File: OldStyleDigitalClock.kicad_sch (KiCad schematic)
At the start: 81 parts, among them SW1 Set minutes, SW2 Set hours, U1 D168K, U10 D168K, U11 CD4026BE, U12 D168K, U13 CD4026BE, U2 CD4026BE, U3 CD4060BE, U4 D168K, U5 CD4026BE, U6 CD4017BE, U7 CD4017BE, U8 CD4017BE, U9 4073, Y1 HC49 XTAL (32768 Hz)

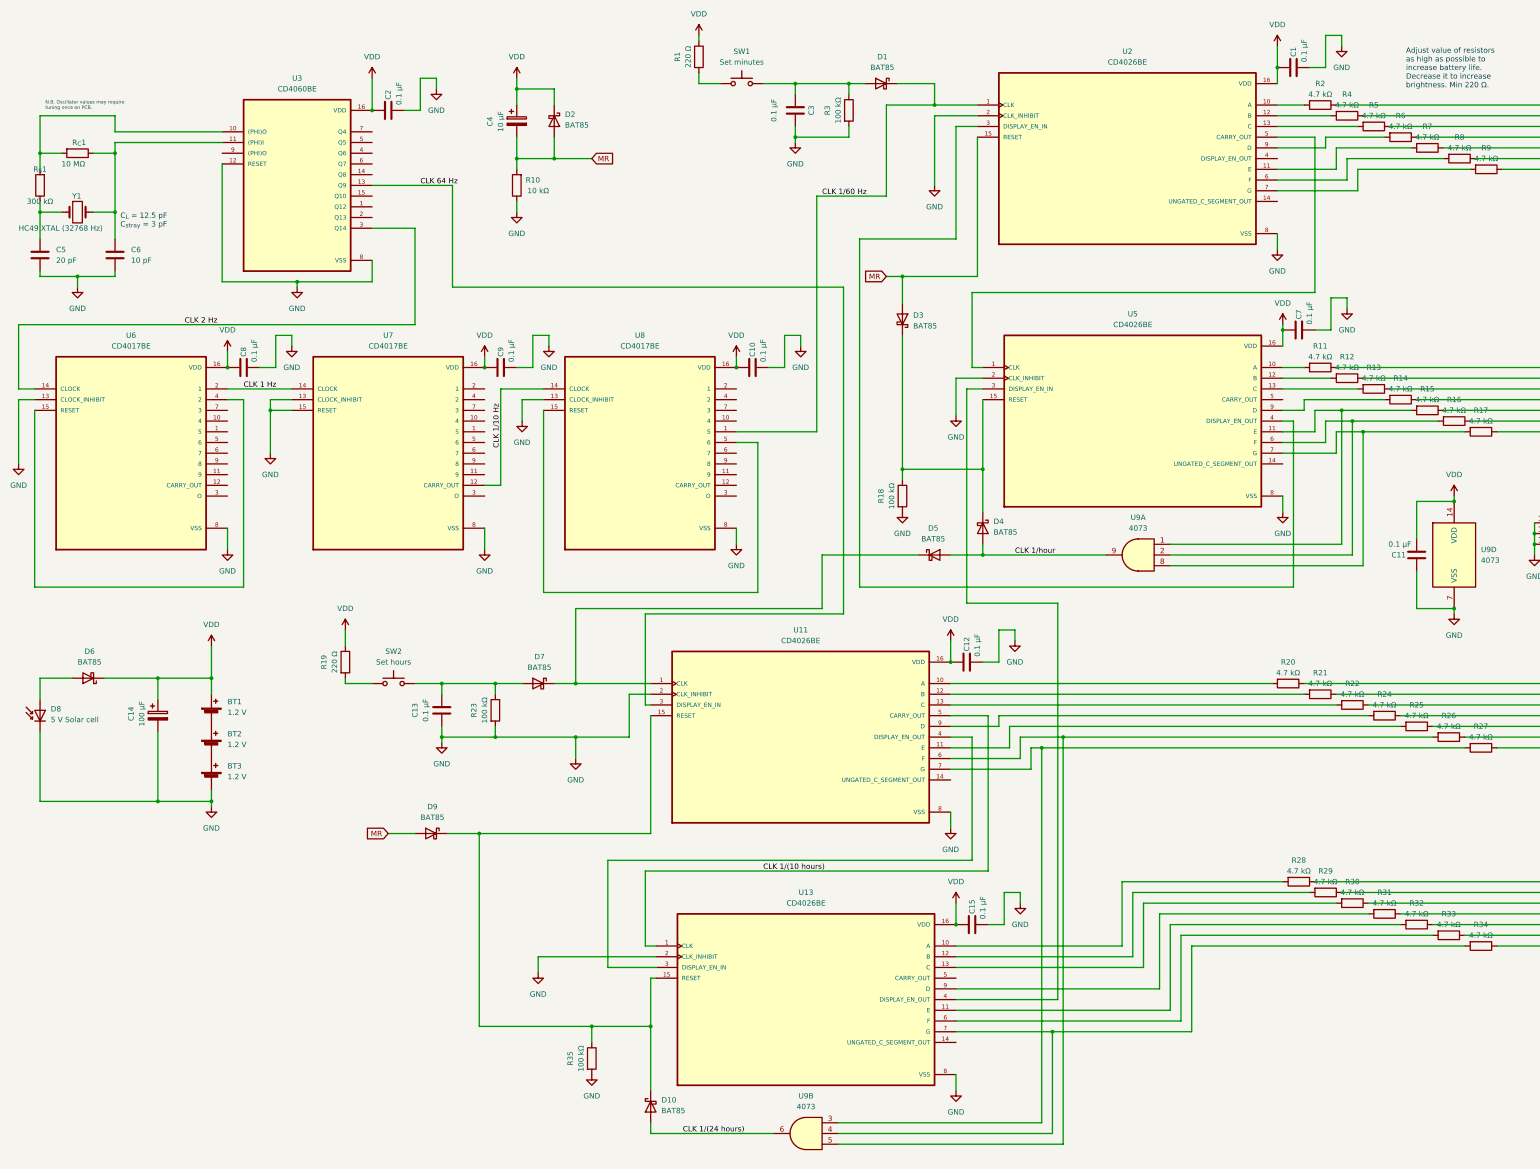
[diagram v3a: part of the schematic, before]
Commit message: Removed batteries and added USB connectors. One USB C for power in, two usb A power outlets. Pre-routing.
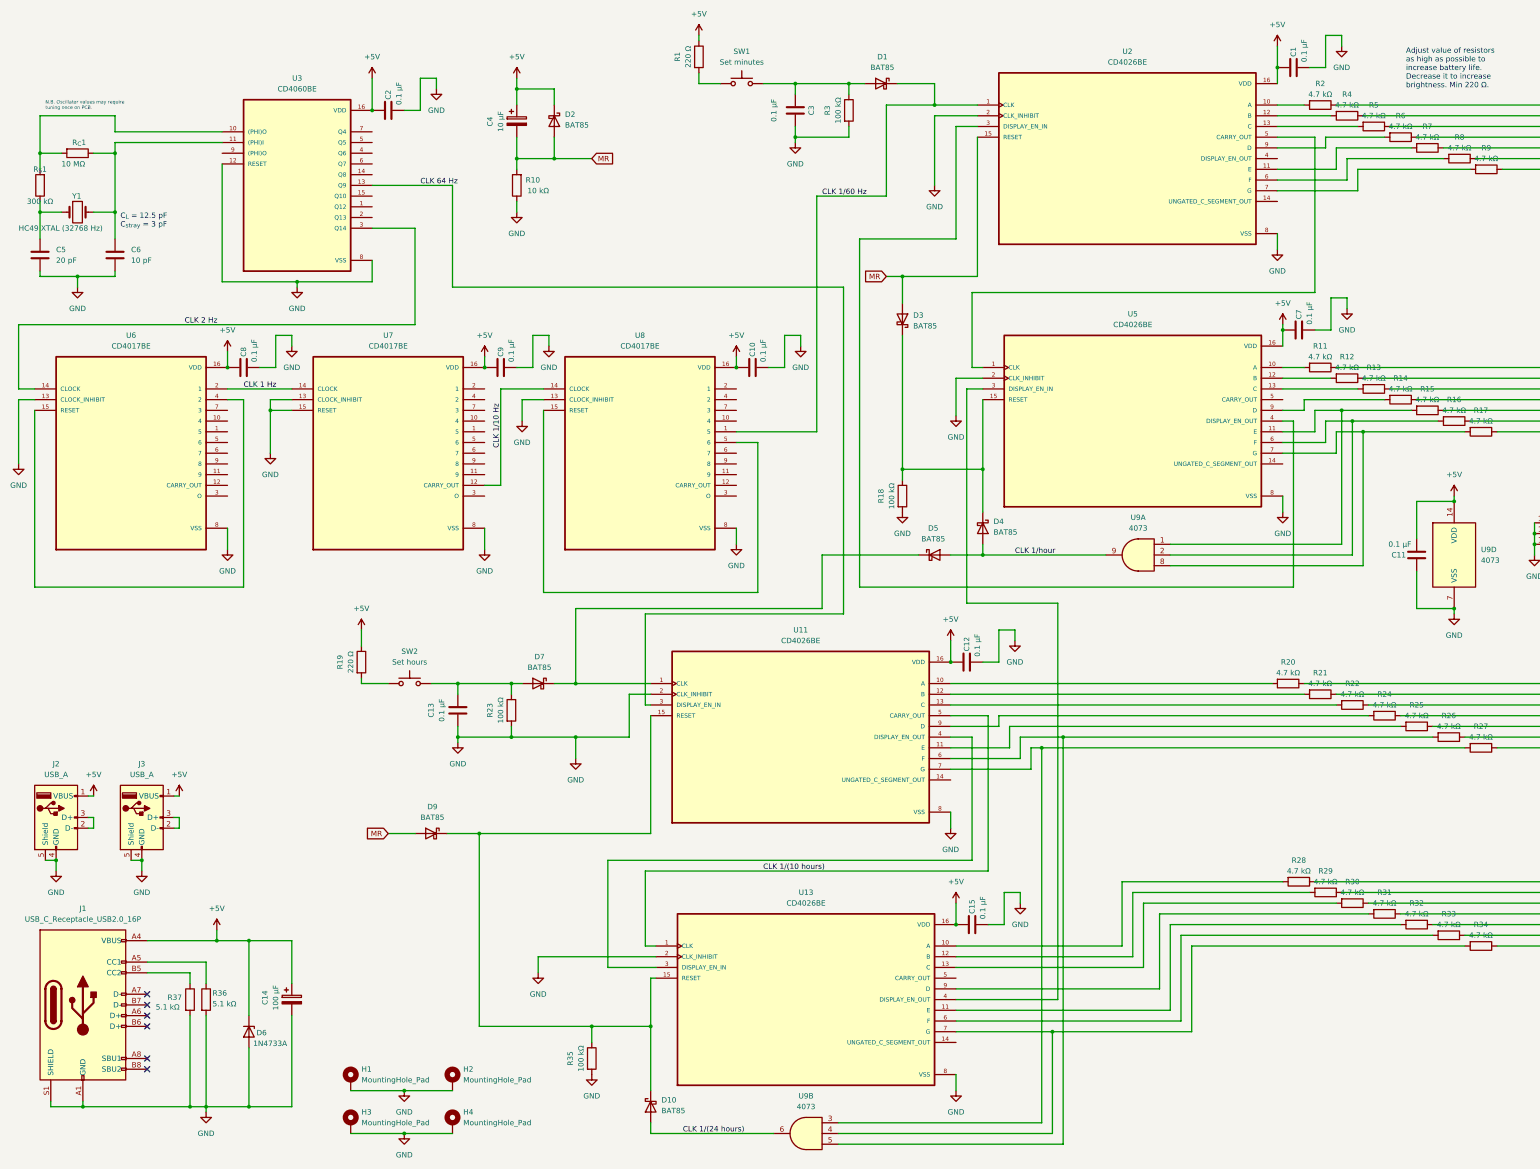
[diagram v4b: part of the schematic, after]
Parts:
- removed BT1, BT2, BT3: 1.2 V, CustomLibrary:AA battery holder, symbol Device:Battery_Cell
- removed D6: BAT85, Diode_THT:D_DO-35_SOD27_P7.62mm_Horizontal, symbol Diode:BAT85
- removed D8: 5 V Solar cell, TerminalBlock:TerminalBlock_bornier-2_P5.08mm, symbol Device:D_Photo
- added D6: 1N4733A, Diode_THT:D_DO-35_SOD27_P7.62mm_Horizontal, symbol Device:D_Zener
- added H1, H2, H3, H4: MountingHole_Pad, MountingHole:MountingHole_2.2mm_M2_DIN965, symbol Mechanical:MountingHole_Pad
- added J1: USB_C_Receptacle_USB2.0_16P, Connector_USB:USB_C_Receptacle_GCT_USB4110, symbol Connector:USB_C_Receptacle_USB2.0_16P
- added J2, J3: USB_A, Connector_USB:USB_A_Molex_67643_Horizontal, symbol Connector:USB_A
- added R36, R37: 5.1 kΩ, Resistor_THT:R_Axial_DIN0204_L3.6mm_D1.6mm_P7.62mm_Horizontal, symbol Device:R
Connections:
- net GND: now also D6.2 (A), H1.1, H2.1, H3.1, H4.1, J1.A1 (GND), J1.A12 (GND), J1.B1 (GND), J1.B12 (GND), J1.S1 (SHIELD), J2.4 (GND), J2.5 (Shield), J3.4 (GND), J3.5 (Shield), R36.2, R37.2
- net VDD renamed +5V
- net +5V: now also D6.1 (K), J1.A4 (VBUS), J1.A9 (VBUS), J1.B4 (VBUS), J1.B9 (VBUS), J2.1 (VBUS), J3.1 (VBUS)
- new net: J1.B5 (CC2), R37.1
- new net: J1.A5 (CC1), R36.1
- new net: J2.2 (D-), J2.3 (D+)
- new net: J3.2 (D-), J3.3 (D+)
- no-connect marks 0 -> 6
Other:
- moved on the sheet: C13, C14, R19, R23, SW2

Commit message: Introducing PWM for dimmable LEDs
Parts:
- removed C10, C2, C8, C9: 0.1 µF, Capacitor_THT:C_Disc_D5.1mm_W3.2mm_P5.00mm, symbol Device:C
- removed C14: 100 µF, Capacitor_THT:CP_Radial_D6.3mm_P2.50mm, symbol Device:C_Polarized
- removed C4: 10 µF, Capacitor_THT:CP_Radial_D6.3mm_P2.50mm, symbol Device:C_Polarized
- removed C5: 20 pF, Capacitor_THT:C_Disc_D5.1mm_W3.2mm_P5.00mm, symbol Device:C
- removed C6: 10 pF, Capacitor_THT:C_Disc_D5.1mm_W3.2mm_P5.00mm, symbol Device:C
- removed D2, D5: BAT85, Diode_THT:D_DO-35_SOD27_P7.62mm_Horizontal, symbol Diode:BAT85
- removed D6: 1N4733A, Diode_THT:D_DO-35_SOD27_P7.62mm_Horizontal, symbol Device:D_Zener
- removed H1, H2, H3, H4: MountingHole_Pad, MountingHole:MountingHole_2.2mm_M2_DIN965, symbol Mechanical:MountingHole_Pad
- removed J1: USB_C_Receptacle_USB2.0_16P, Connector_USB:USB_C_Receptacle_GCT_USB4110, symbol Connector:USB_C_Receptacle_USB2.0_16P
- removed J2, J3: USB_A, Connector_USB:USB_A_Molex_67643_Horizontal, symbol Connector:USB_A
- removed R10: 10 kΩ, Resistor_THT:R_Axial_DIN0204_L3.6mm_D1.6mm_P7.62mm_Horizontal, symbol Device:R
- removed R36, R37: 5.1 kΩ, Resistor_THT:R_Axial_DIN0204_L3.6mm_D1.6mm_P7.62mm_Horizontal, symbol Device:R
- removed R_{C}1: 10 MΩ, Resistor_THT:R_Axial_DIN0204_L3.6mm_D1.6mm_P7.62mm_Horizontal, symbol Device:R
- removed R_{S}1: 300 kΩ, Resistor_THT:R_Axial_DIN0204_L3.6mm_D1.6mm_P7.62mm_Horizontal, symbol Device:R
- removed U3: CD4060BE, CD4060BE:DIP794W45P254L1969H508Q16, symbol CD4060BE:CD4060BE
- removed U6, U7, U8: CD4017BE, CD4017BE:DIP794W45P254L1969H508Q16, symbol CD4017BE:CD4017BE
- removed Y1: HC49 XTAL (32768 Hz), Crystal:Crystal_AT310_D3.0mm_L10.0mm_Horizontal, symbol Device:Crystal
- added R38: 100 kΩ, Resistor_THT:R_Axial_DIN0204_L3.6mm_D1.6mm_P7.62mm_Horizontal, symbol Device:R
- R11, R12, R13, R14, R15, R16, R17, R2, R20, R21, R22, R24, R25, R26, R27, R28, R29, R30, R31, R32, R33, R34, R4, R5, R6, R7, R8, R9: value 4.7 kΩ -> 2.2 kΩ
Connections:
- net CLK 1/hour: now also D7.1 (K), U11.1 (CLK)
- net GND: now also R38.2
- net MR: now also R38.1
- net CLK 1/60 Hz renamed 1_MIN_CLK
- net CLK 64 Hz renamed LED_PWM
- no-connect marks 6 -> 1
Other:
- added sheet Power (OldStyleDigitalClock_power.kicad_sch)
- added sheet Time (OldStyleDigitalClock_time.kicad_sch)
- note added: "Adjust value of resistors as high as possible to increase battery life. Decrease it to increase brightness. Min. 220 Ω."
- note removed: "Adjust value of resistors as high as possible to increase battery life. Decrease it to increase brightness. Min 220 Ω."
- note removed: "C_{L} = 12.5 pF C_{stray} = 3 pF"
- note removed: "N.B. Oscillator values may require tuning once on PCB."
- moved on the sheet: C13, C3, D1, D3, D7, R1, R18, R19, R23, R3, SW1, SW2

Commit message: Comment
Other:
- note added: "Value of resistors may need to be adjusted according to the chosen 7 segment LEDs."
- note removed: "Adjust value of resistors as high as possible to increase battery life. Decrease it to increase brightness. Min. 220 Ω."
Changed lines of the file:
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@@
 		(company "Pasquale Lafiosca")
 	)
-	(text "Adjust value of resistors\nas high as possible to\nincrease battery life.\nDecrease it to increase\nbrightness. Min. 220 Ω. "
+	(text "Value of resistors may need\nto be adjusted according to\nthe chosen 7 segment LEDs."
 		(exclude_from_sim no)
 		(at 345.44 30.48 0)

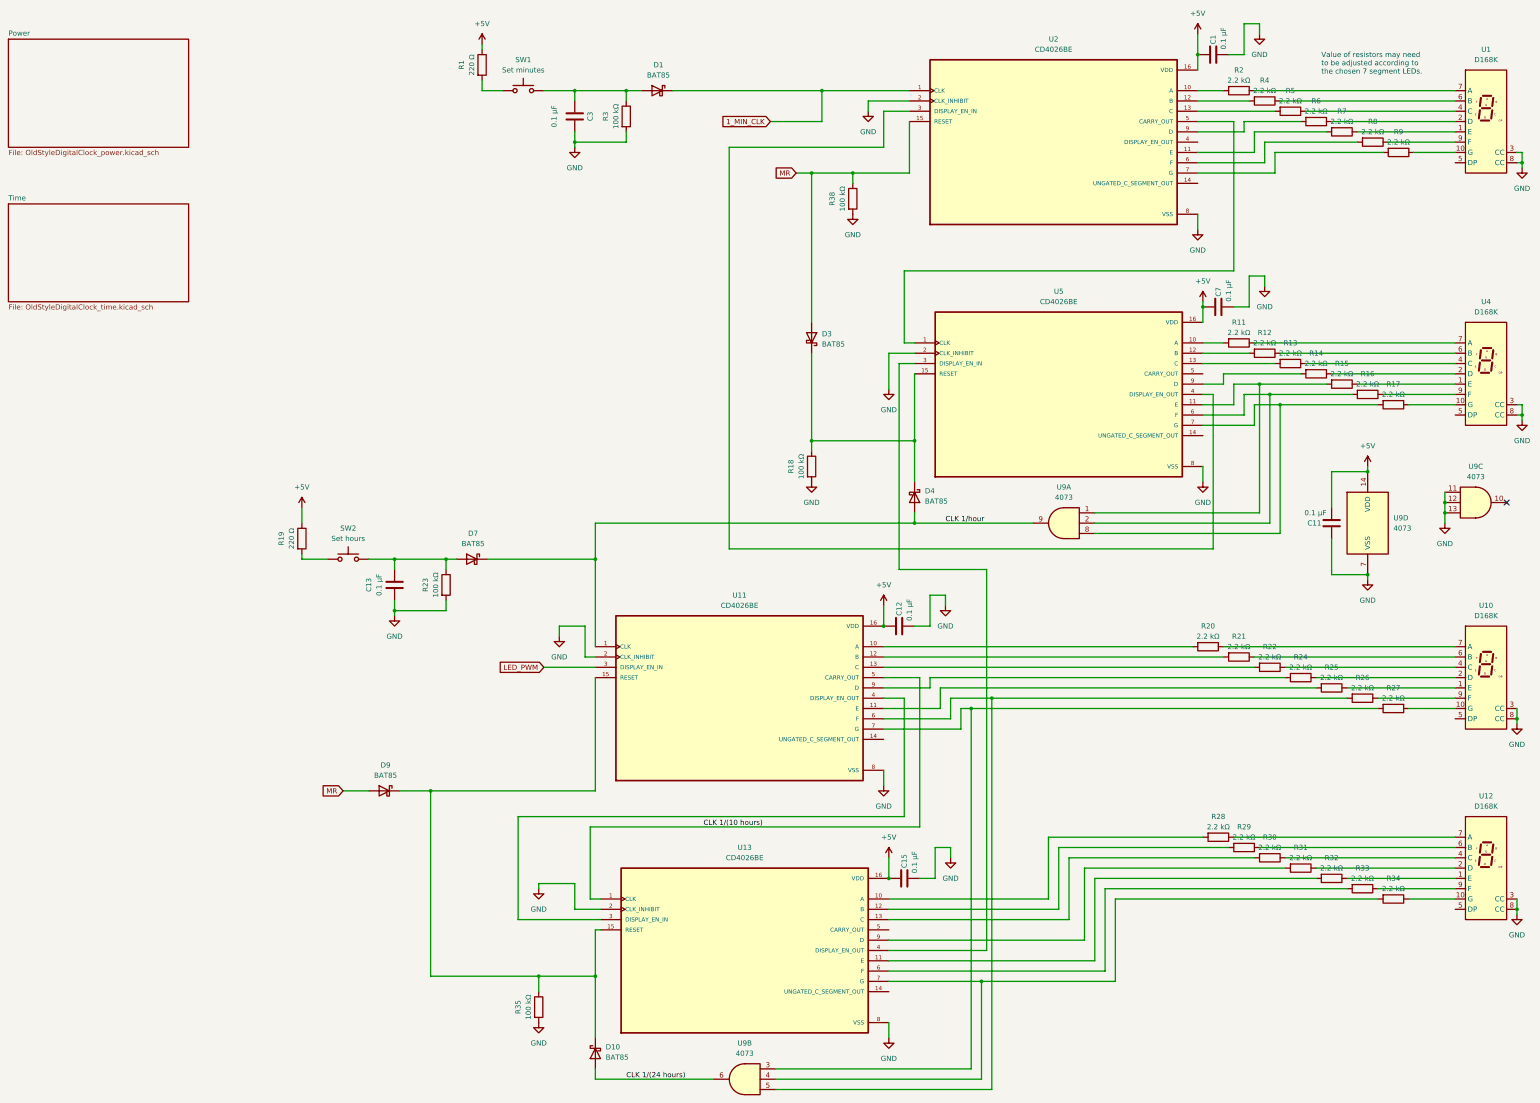
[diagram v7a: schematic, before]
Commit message: Using OR gates instead of diodes. Changed POT for 555
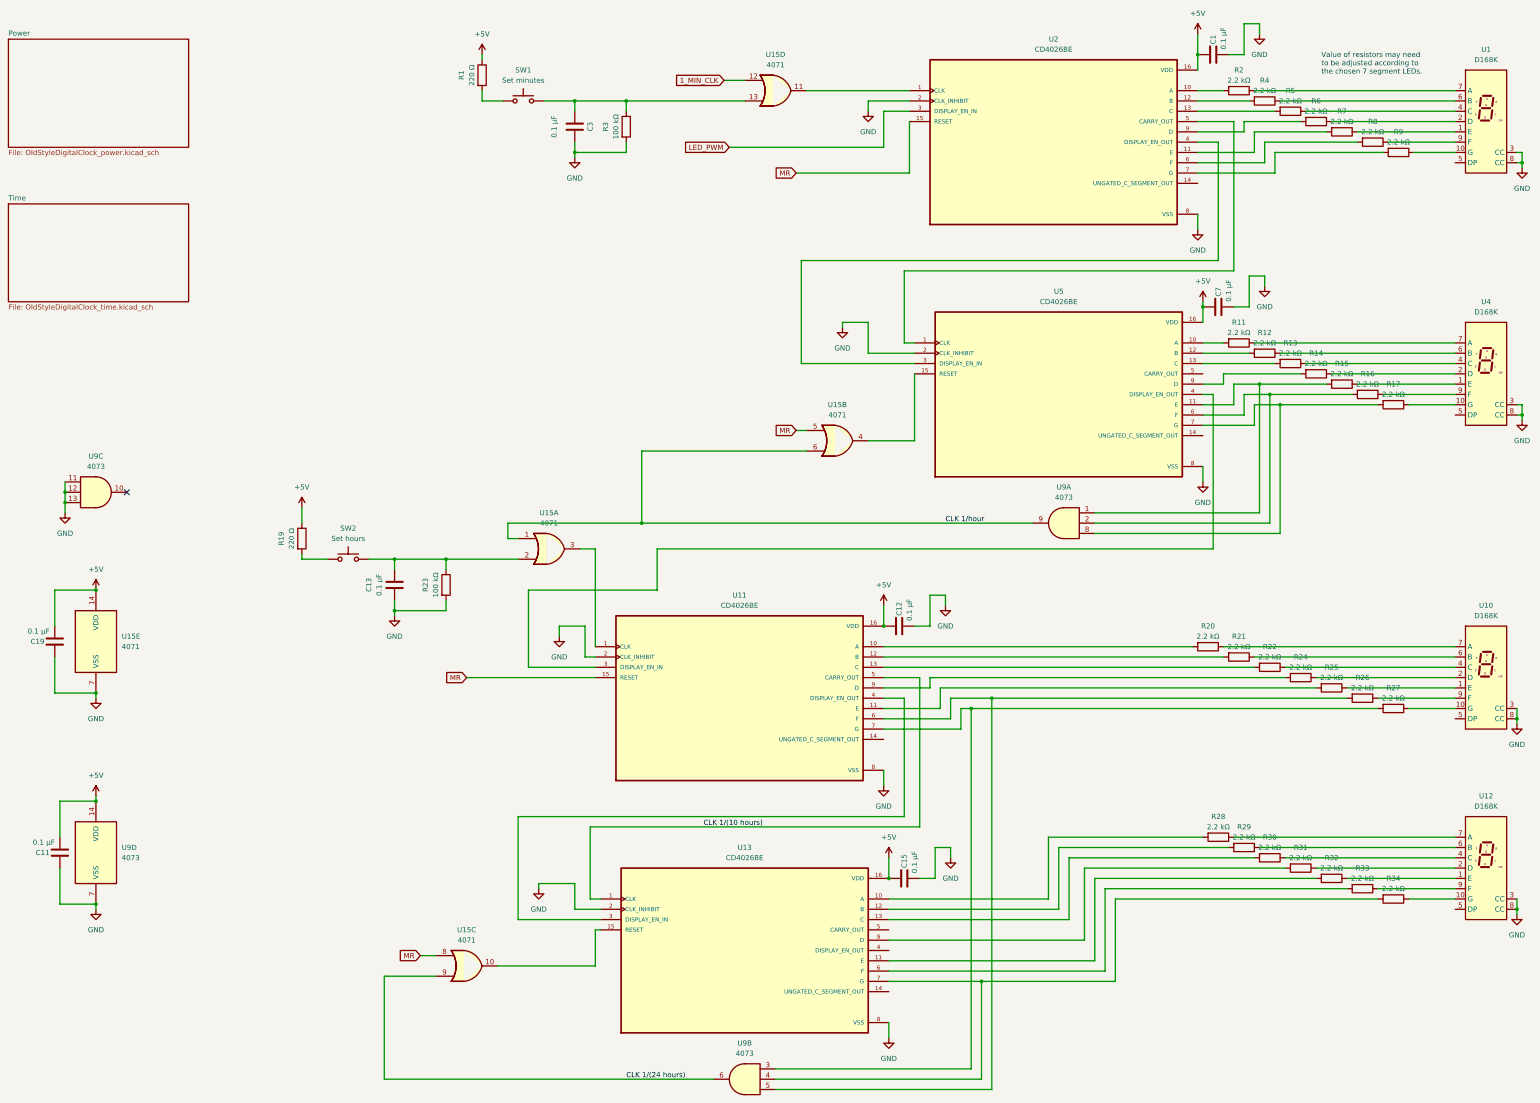
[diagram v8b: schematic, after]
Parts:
- removed D1, D10, D3, D4, D7, D9: BAT85, Diode_THT:D_DO-35_SOD27_P7.62mm_Horizontal, symbol Diode:BAT85
- removed R18, R35, R38: 100 kΩ, Resistor_THT:R_Axial_DIN0204_L3.6mm_D1.6mm_P7.62mm_Horizontal, symbol Device:R
- added C19: 0.1 µF, Capacitor_THT:C_Disc_D5.1mm_W3.2mm_P5.00mm, symbol Device:C
- added U15: 4071, symbol 4xxx:4071
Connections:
- net +5V: now also C19.2, U15.14 (VDD)
- net 1_MIN_CLK: now also U15.12; no longer U2.1 (CLK)
- net CLK 1/(24 hours): now also U15.9
- net CLK 1/hour: now also U15.1, U15.6; no longer U11.1 (CLK)
- net GND: now also C19.1, U15.7 (VSS)
- net LED_PWM: now also U2.3 (DISPLAY_EN_IN); no longer U11.3 (DISPLAY_EN_IN)
- net MR: now also U11.15 (RESET), U15.5, U15.8
- net at U13.15 (RESET): now also U15.10; no longer U11.15 (RESET)
- net at U5.15 (RESET): now also U15.4
- net at C13.2, R23.1, SW2.2: now also U15.2
- net at C3.2, R3.1, SW1.2: now also U15.13
- net at U5.4 (DISPLAY_EN_OUT): now also U11.3 (DISPLAY_EN_IN); no longer U2.3 (DISPLAY_EN_IN)
- net at U2.4 (DISPLAY_EN_OUT): now also U5.3 (DISPLAY_EN_IN)
- net at U13.4 (DISPLAY_EN_OUT): no longer U5.3 (DISPLAY_EN_IN)
- new net: U11.1 (CLK), U15.3
- new net: U15.11, U2.1 (CLK)
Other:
- moved on the sheet: C11, C3, R1, R3, SW1, U9C, U9D
